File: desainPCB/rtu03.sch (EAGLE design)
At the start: 13 parts, among them M1 ARDUINO-PRO-MINI-5.0V, X1 JST-XH-02-PIN-LONG-PAD

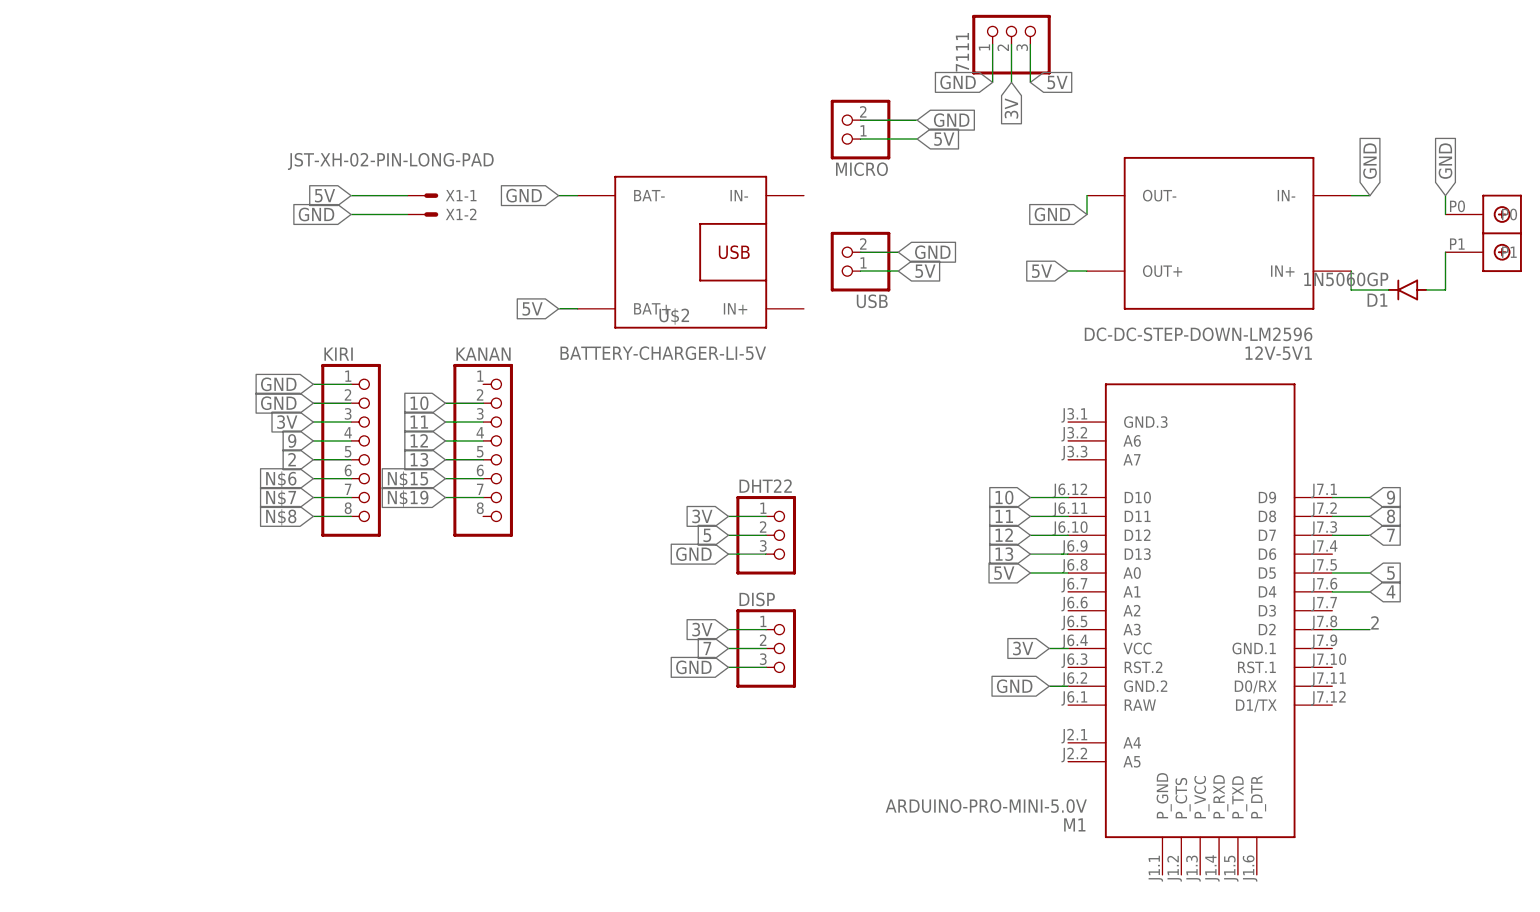
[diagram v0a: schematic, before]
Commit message: new sensor suhu
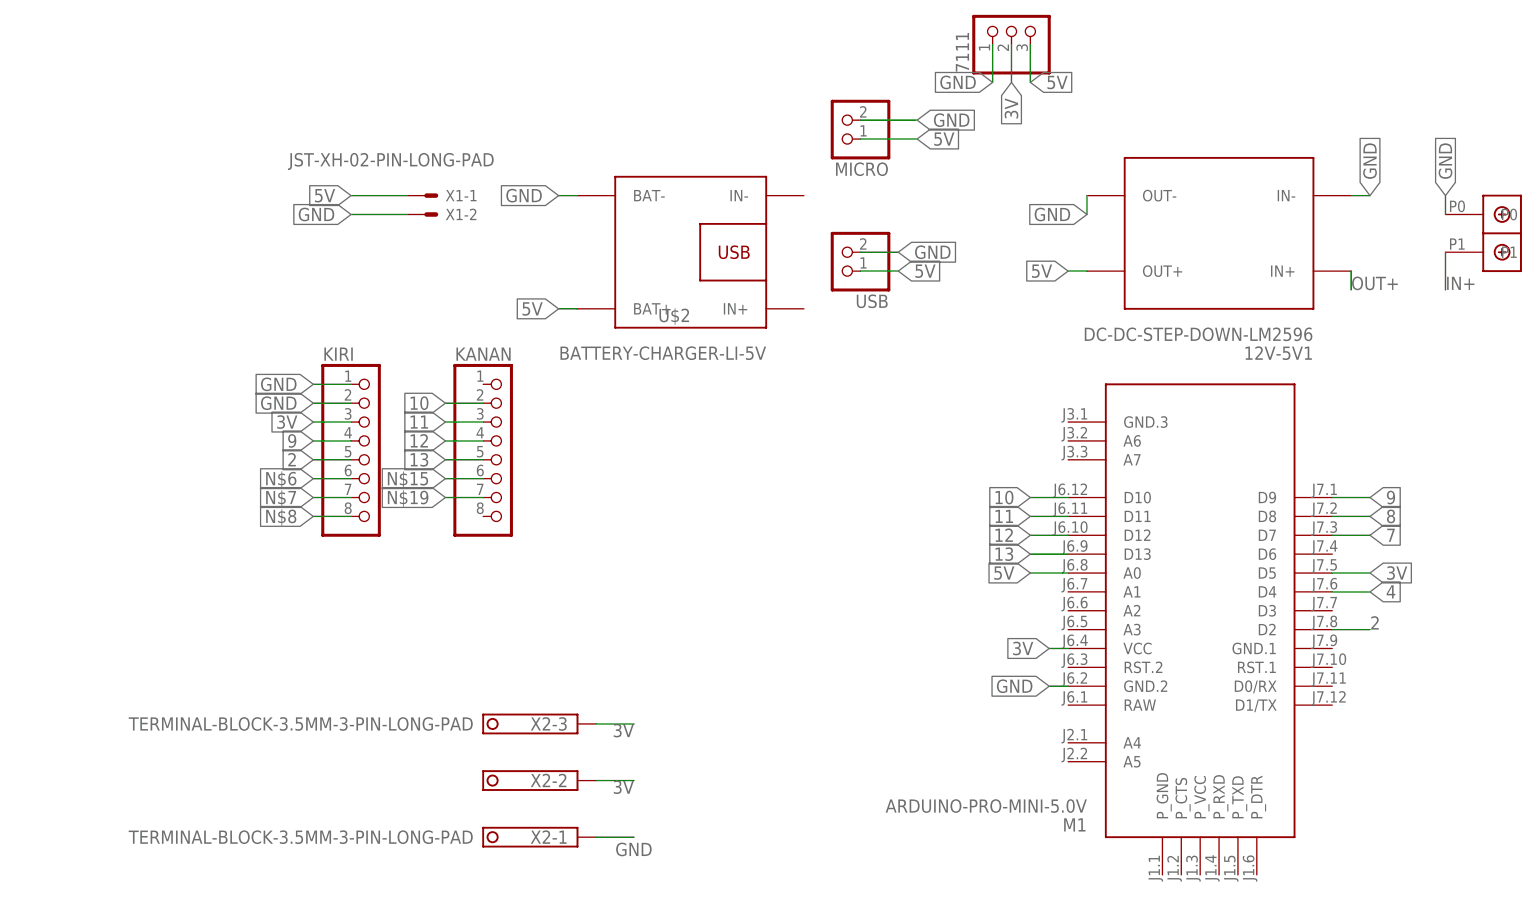
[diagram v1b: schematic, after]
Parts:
- removed D1: 1N5060GP, diode:1N5060GP
- removed DHT22, DISP: (no value), pinhead:PINHD-1X3
- added X2: TERMINAL-BLOCK-3.5MM-3-PIN-LONG-PAD, Rembrandt Electronics - Terminal Block 3-5mm v1-0:TERMINAL-BLOCK-3.5MM-3-PIN-LONG-PAD
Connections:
- removed net 5: DHT22.2, M1.D5
- removed net N$1: D1.A, U$1.P1
- removed net N$2: 12V-5V1.IN+, D1.C
- new net IN+: U$1.P1
- new net OUT+: 12V-5V1.IN+
- net 3V: now also M1.D5, X2-2.K, X2-3.K; no longer DHT22.1, DISP.1
- net 7: no longer DISP.2
- net GND: now also X2-1.K; no longer DHT22.3, DISP.3
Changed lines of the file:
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@@
 <part name="KIRI" library="pinhead" library_urn="urn:adsk.eagle:library:325" deviceset="PINHD-1X8" device="" package3d_urn="urn:adsk.eagle:package:22409/2"/>
 <part name="7111" library="pinhead" library_urn="urn:adsk.eagle:library:325" deviceset="PINHD-1X3" device="" package3d_urn="urn:adsk.eagle:package:22458/2"/>
-<part name="DHT22" library="pinhead" library_urn="urn:adsk.eagle:library:325" deviceset="PINHD-1X3" device="" package3d_urn="urn:adsk.eagle:package:22458/2"/>
-<part name="DISP" library="pinhead" library_urn="urn:adsk.eagle:library:325" deviceset="PINHD-1X3" device="" package3d_urn="urn:adsk.eagle:package:22458/2"/>
 <part name="U$2" library="diy-modules (1)" deviceset="BATTERY-CHARGER-LI-5V" device=""/>
 <part name="MICRO" library="pinhead" library_urn="urn:adsk.eagle:library:325" deviceset="PINHD-1X2" device="" package3d_urn="urn:adsk.eagle:package:22435/2"/>
 <part name="USB" library="pinhead" library_urn="urn:adsk.eagle:library:325" deviceset="PINHD-1X2" device="" package3d_urn="urn:adsk.eagle:package:22435/2"/>
-<part name="D1" library="diode" library_urn="urn:adsk.eagle:library:210" deviceset="1N5060GP" device="" package3d_urn="urn:adsk.eagle:package:43369/2"/>
+<part name="X2" library="Rembrandt Electronics - Terminal Block 3-5mm v1-0" deviceset="TERMINAL-BLOCK-3.5MM-3-PIN" device="-LONG-PAD"/>
 </parts>
 <sheets>
@@
 <attribute name="VALUE" x="88.9" y="95.25" size="1.778" layer="96" rot="R90"/>
 </instance>
-<instance part="DHT22" gate="A" x="50.8" y="33.02" smashed="yes">
-<attribute name="NAME" x="44.45" y="38.735" size="1.778" layer="95"/>
-<attribute name="VALUE" x="44.45" y="25.4" size="1.778" layer="96"/>
-</instance>
-<instance part="DISP" gate="A" x="50.8" y="17.78" smashed="yes">
-<attribute name="NAME" x="44.45" y="23.495" size="1.778" layer="95"/>
-<attribute name="VALUE" x="44.45" y="10.16" size="1.778" layer="96"/>
-</instance>
 <instance part="U$2" gate="G$1" x="38.1" y="71.12" smashed="yes" rot="R180">
 <attribute name="NAME" x="38.1" y="63.5" size="1.778" layer="95" rot="R180"/>
@@
 <attribute name="VALUE" x="64.77" y="76.2" size="1.778" layer="96" rot="R180"/>
 </instance>
-<instance part="D1" gate="1" x="134.62" y="66.04" smashed="yes" rot="R180">
-<attribute name="NAME" x="132.08" y="65.5574" size="1.778" layer="95" rot="R180"/>
-<attribute name="VALUE" x="132.08" y="68.3514" size="1.778" layer="96" rot="R180"/>
+<instance part="X2" gate="-1" x="22.86" y="-7.62" smashed="yes" rot="R180">
+<attribute name="NAME" x="21.59" y="-6.731" size="1.778" layer="95" rot="R180"/>
+<attribute name="VALUE" x="8.89" y="-6.731" size="1.778" layer="96" rot="R180"/>
+</instance>
+<instance part="X2" gate="-2" x="22.86" y="0" smashed="yes" rot="R180">
+<attribute name="NAME" x="21.59" y="0.889" size="1.778" layer="95" rot="R180"/>
+</instance>
+<instance part="X2" gate="-3" x="22.86" y="7.62" smashed="yes" rot="R180">
+<attribute name="NAME" x="21.59" y="8.509" size="1.778" layer="95" rot="R180"/>
+<attribute name="VALUE" x="8.89" y="8.509" size="1.778" layer="96" rot="R180"/>
 </instance>
 </instances>
@@
 </segment>
 <segment>
-<pinref part="DHT22" gate="A" pin="3"/>
-<wire x1="48.26" y1="30.48" x2="43.18" y2="30.48" width="0.1524" layer="91"/>
-<label x="43.18" y="30.48" size="1.778" layer="95" rot="R180" xref="yes"/>
-</segment>
-<segment>
-<pinref part="DISP" gate="A" pin="3"/>
-<wire x1="48.26" y1="15.24" x2="43.18" y2="15.24" width="0.1524" layer="91"/>
-<label x="43.18" y="15.24" size="1.778" layer="95" rot="R180" xref="yes"/>
-</segment>
-<segment>
 <wire x1="20.32" y1="78.74" x2="22.86" y2="78.74" width="0.1524" layer="91"/>
 <label x="20.32" y="78.74" size="1.778" layer="95" rot="R180" xref="yes"/>
@@
 <label x="66.04" y="71.12" size="1.778" layer="95" xref="yes"/>
 </segment>
+<segment>
+<pinref part="X2" gate="-1" pin="K"/>
+<wire x1="25.4" y1="-7.62" x2="30.48" y2="-7.62" width="0.1524" layer="91"/>
+<label x="27.94" y="-10.16" size="1.778" layer="95"/>
+</segment>
 </net>
 <net name="3V" class="0">
@@
 </segment>
 <segment>
-<pinref part="DHT22" gate="A" pin="1"/>
-<wire x1="48.26" y1="35.56" x2="43.18" y2="35.56" width="0.1524" layer="91"/>
-<label x="43.18" y="35.56" size="1.778" layer="95" rot="R180" xref="yes"/>
-</segment>
-<segment>
-<pinref part="DISP" gate="A" pin="1"/>
-<wire x1="48.26" y1="20.32" x2="43.18" y2="20.32" width="0.1524" layer="91"/>
-<label x="43.18" y="20.32" size="1.778" layer="95" rot="R180" xref="yes"/>
-</segment>
-<segment>
 <pinref part="M1" gate="G$1" pin="VCC"/>
 <wire x1="88.9" y1="17.78" x2="86.36" y2="17.78" width="0.1524" layer="91"/>
 <label x="86.36" y="17.78" size="1.778" layer="95" rot="R180" xref="yes"/>
 </segment>
+<segment>
+<pinref part="X2" gate="-3" pin="K"/>
+<wire x1="25.4" y1="7.62" x2="30.48" y2="7.62" width="0.1524" layer="91"/>
+<label x="30.48" y="7.62" size="1.778" layer="95" rot="R180"/>
+</segment>
+<segment>
+<pinref part="X2" gate="-2" pin="K"/>
+<wire x1="25.4" y1="0" x2="30.48" y2="0" width="0.1524" layer="91"/>
+<label x="30.48" y="0" size="1.778" layer="95" rot="R180"/>
+</segment>
+<segment>
+<pinref part="M1" gate="G$1" pin="D5"/>
+<wire x1="124.46" y1="27.94" x2="129.54" y2="27.94" width="0.1524" layer="91"/>
+<label x="129.54" y="27.94" size="1.778" layer="95" xref="yes"/>
+</segment>
 </net>
 <net name="5V" class="0">
@@
 <label x="129.54" y="33.02" size="1.778" layer="95" xref="yes"/>
 </segment>
-<segment>
-<pinref part="DISP" gate="A" pin="2"/>
-<wire x1="48.26" y1="17.78" x2="43.18" y2="17.78" width="0.1524" layer="91"/>
-<label x="43.18" y="17.78" size="1.778" layer="95" rot="R180" xref="yes"/>
-</segment>
 </net>
 <net name="N$6" class="0">
@@
 </segment>
 </net>
-<net name="5" class="0">
-<segment>
-<pinref part="DHT22" gate="A" pin="2"/>
-<wire x1="48.26" y1="33.02" x2="43.18" y2="33.02" width="0.1524" layer="91"/>
-<label x="43.18" y="33.02" size="1.778" layer="95" rot="R180" xref="yes"/>
-</segment>
-<segment>
-<pinref part="M1" gate="G$1" pin="D5"/>
-<wire x1="124.46" y1="27.94" x2="129.54" y2="27.94" width="0.1524" layer="91"/>
-<label x="129.54" y="27.94" size="1.778" layer="95" xref="yes"/>
-</segment>
-</net>
 <net name="9" class="0">
 <segment>
@@
 </segment>
 </net>
-<net name="N$1" class="0">
-<segment>
-<pinref part="D1" gate="1" pin="A"/>
-<wire x1="137.16" y1="66.04" x2="139.7" y2="66.04" width="0.1524" layer="91"/>
+<net name="IN+" class="0">
+<segment>
 <pinref part="U$1" gate="G$1" pin="P1"/>
 <wire x1="139.7" y1="66.04" x2="139.7" y2="71.12" width="0.1524" layer="91"/>
-</segment>
-</net>
-<net name="N$2" class="0">
+<label x="139.7" y="66.04" size="1.778" layer="95"/>
+</segment>
+</net>
+<net name="OUT+" class="0">
 <segment>
 <pinref part="12V-5V1" gate="G$1" pin="IN+"/>
 <wire x1="127" y1="68.58" x2="127" y2="66.04" width="0.1524" layer="91"/>
-<pinref part="D1" gate="1" pin="C"/>
-<wire x1="127" y1="66.04" x2="132.08" y2="66.04" width="0.1524" layer="91"/>
-</segment>
-</net>
+<label x="127" y="66.04" size="1.778" layer="95"/>
+</segment>
+</net>
